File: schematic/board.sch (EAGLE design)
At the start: 4 parts, among them U1 STM32F103C8T6

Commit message: Кажется, все необходимое для МК нарисовано
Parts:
- added C1: 10uF, SparkFun-Capacitors:10UF-1206-6.3V-20%
- added C2: 100uF, SparkFun-Capacitors:10UF-1206-6.3V-20%
- added C3, C4: 8uF, SparkFun-Capacitors:22UF-0805-6.3V-20%
- added C5, C6: 7uF, SparkFun-Capacitors:22UF-0805-6.3V-20%
- added R1: 1.5kOhm, rcl:R-EU_R0603
- added R2: 0 Ohm, rcl:R-EU_R0603
- added X1: NX3215SA-32.768K, SparkFun-Clocks:CRYSTALSMD-3.2X1.5
- added X2: NX5032GA-8MHz, SparkFun-Clocks:CRYSTALSMD-5X3.2-2PAD
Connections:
- new net N$1: C4.2, U1.PD0_OSC_IN, X2.1
- new net N$2: R1.2, U1.PD1_OSC_OUT
- new net N$3: C6.1, R2.2, X1.1
- new net N$4: C3.2, R1.1, X2.2
- new net N$5: C5.1, U1.PC14-OSC32_IN, X1.2
- new net N$6: R2.1, U1.PC15-OSC32_OUT
- net +3V3: now also C1.1
- net +5V: now also C2.1
- net GND: now also C1.2, C2.2, C3.1, C4.1, C5.2, C6.2
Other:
- note added: "Все SMD конденсаторы в корпусахх 1206"

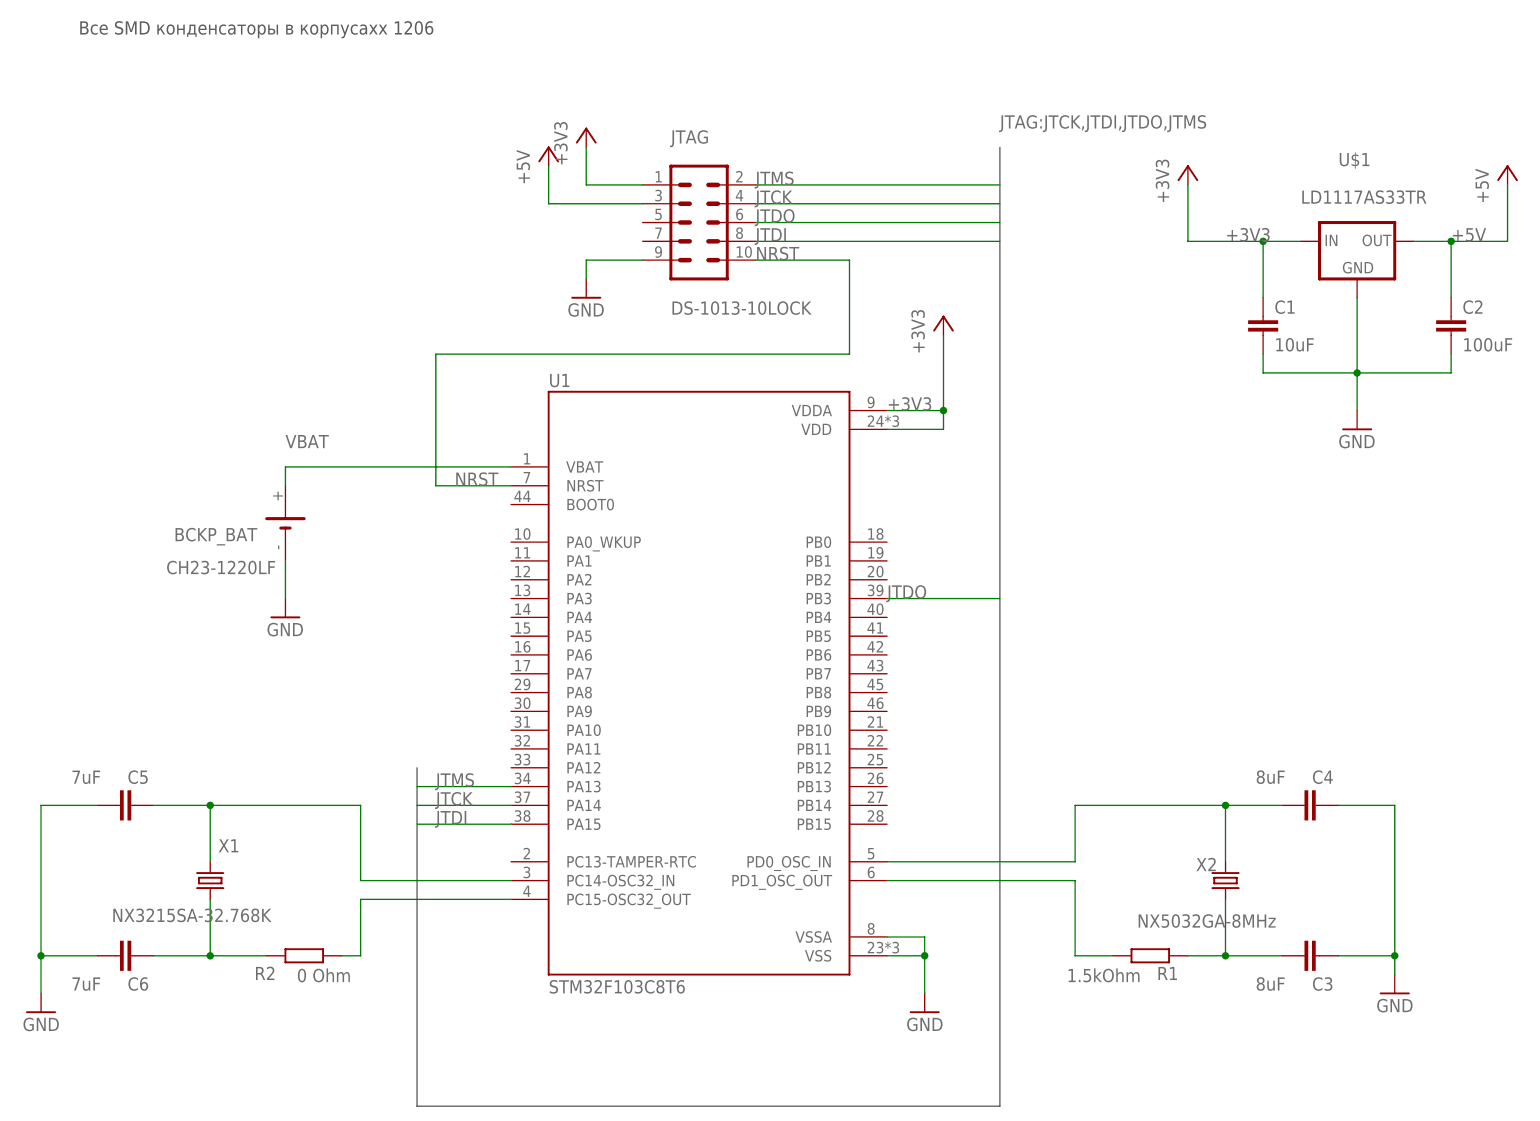
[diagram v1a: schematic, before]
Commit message: Начерно набросана обвязка мк (без фильтрующих кондеров). Обвязка МК нагло срисована с блюпила без номиналов
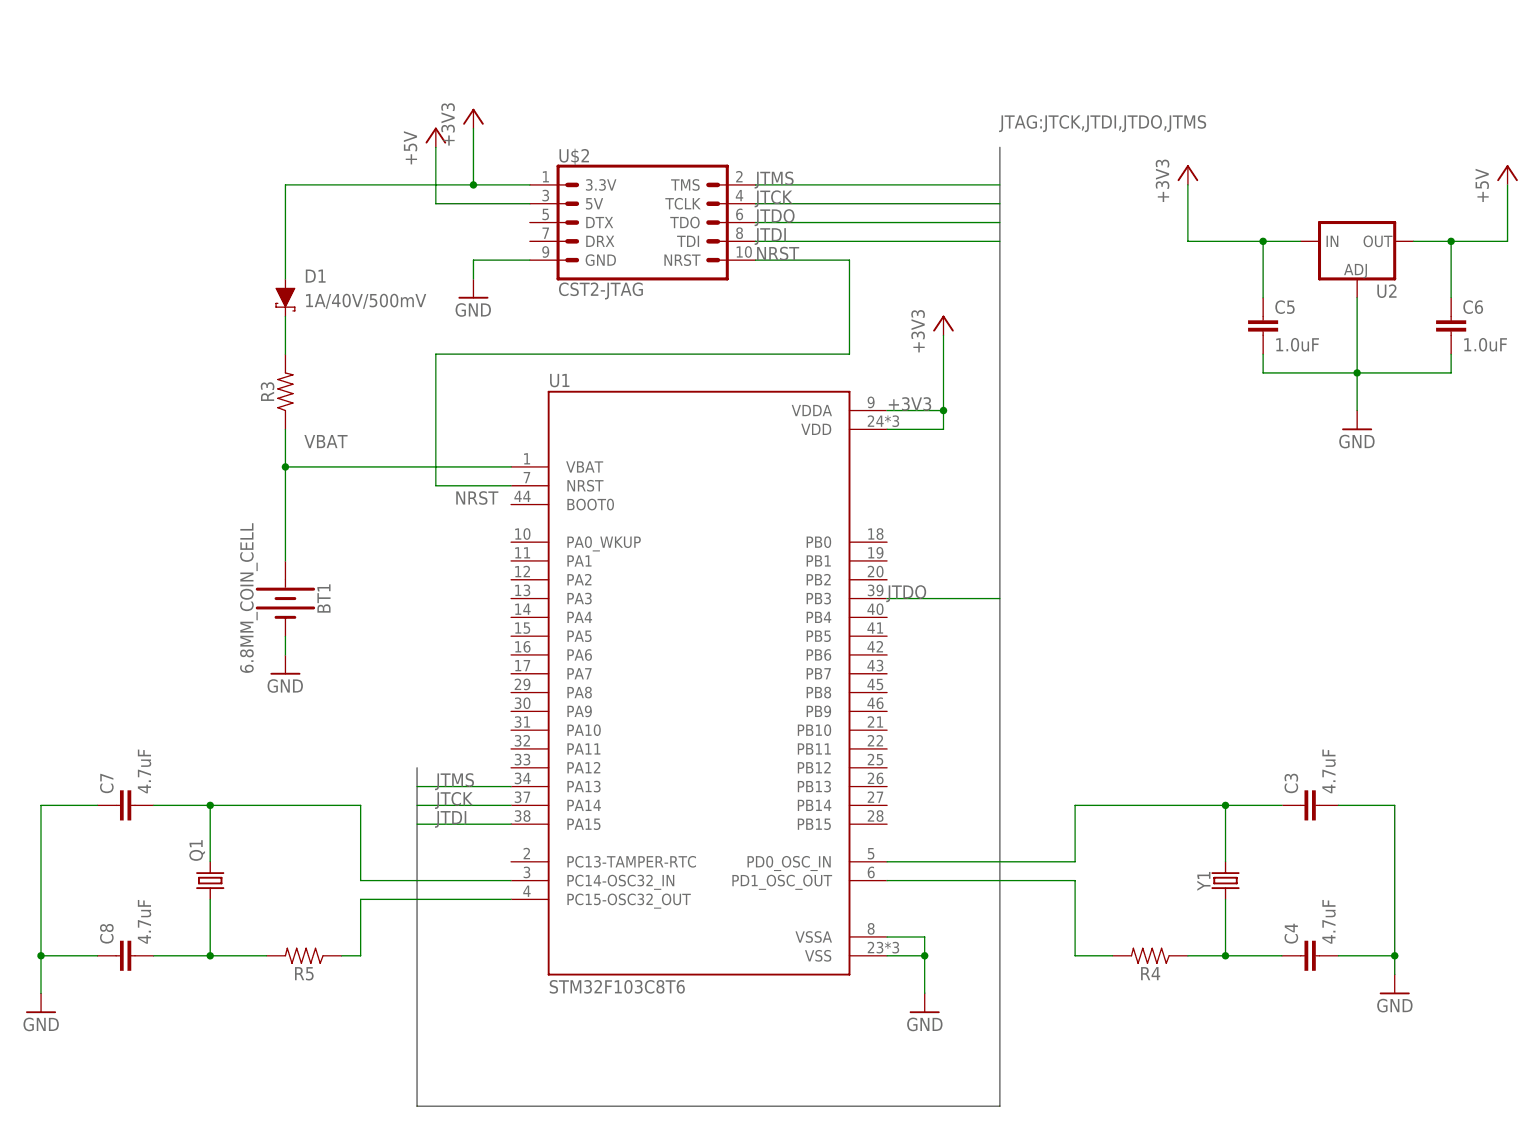
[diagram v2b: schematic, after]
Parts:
- removed BCKP_BAT: CH23-1220LF, battery:CH23-1220LF
- removed C1: 10uF, SparkFun-Capacitors:10UF-1206-6.3V-20%
- removed C2: 100uF, SparkFun-Capacitors:10UF-1206-6.3V-20%
- removed JTAG: DS-1013-10LOCK, IDC:DS-1013-10LOCK
- removed R1: 1.5kOhm, rcl:R-EU_R0603
- removed R2: 0 Ohm, rcl:R-EU_R0603
- removed U$1: LD1117AS33TR, VREG:LD1117AS33TRSOT-223
- removed X1: NX3215SA-32.768K, SparkFun-Clocks:CRYSTALSMD-3.2X1.5
- removed X2: NX5032GA-8MHz, SparkFun-Clocks:CRYSTALSMD-5X3.2-2PAD
- added BT1: 6.8MM_COIN_CELL, SparkFun-Batteries:BATTERY-6.8MM_SMD
- added C7, C8: 4.7uF, SparkFun-Capacitors:4.7UF-0603-35V-(20%)
- added D1: 1A/40V/500mV, SparkFun-DiscreteSemi:DIODE-SCHOTTKY-SS14
- added Q1: (no value), crystal:CRYSTALMM20SS
- added R3, R4, R5: (no value), SparkFun-Resistors:RESISTOR0603
- added U$2: CST2-JTAG, IDC:CST2-JTAG
- added U2: (no value), SparkFun-IC-Power:V_REG_LM1117SOT223
- added Y1: (no value), SparkFun-Clocks:CRYSTALPTH-HC49US
- C3, C4: value 8uF -> 4.7uF; device SparkFun-Capacitors:22UF-0805-6.3V-20% -> SparkFun-Capacitors:4.7UF-0603-35V-(20%)
- C5, C6: value 7uF -> 1.0uF; device SparkFun-Capacitors:22UF-0805-6.3V-20% -> SparkFun-Capacitors:1.0UF-0805-25V-10%
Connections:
- new net N$7: D1.C, R3.2
- net +3V3: now also C5.1, D1.A, U$2.3.3V, U2.IN; no longer C1.1, JTAG.1, U$1.IN
- net +5V: now also C6.1, U$2.5V, U2.OUT; no longer C2.1, JTAG.3, U$1.OUT
- net GND: now also BT1.-, C3.2, C4.2, C7.1, C8.1, U$2.GND, U2.ADJ; no longer BCKP_BAT.-, C1.2, C2.2, C3.1, C4.1, JTAG.9, U$1.GND
- net JTCK: now also U$2.TCLK; no longer JTAG.4
- net JTDI: now also U$2.TDI; no longer JTAG.8
- net JTDO: now also U$2.TDO; no longer JTAG.6
- net JTMS: now also U$2.TMS; no longer JTAG.2
- net N$1: now also C3.1, Y1.2; no longer C4.2, X2.1
- net N$2: now also R4.2; no longer R1.2
- net N$3: now also C8.2, Q1.1, R5.2; no longer C6.1, R2.2, X1.1
- net N$4: now also C4.1, R4.1, Y1.1; no longer C3.2, R1.1, X2.2
- net N$5: now also C7.2, Q1.2; no longer C5.1, X1.2
- net N$6: now also R5.1; no longer R2.1
- net NRST: now also U$2.NRST; no longer JTAG.10
- net VBAT: now also BT1.+, R3.1; no longer BCKP_BAT.+
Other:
- note removed: "Все SMD конденсаторы в корпусахх 1206"
- moved on the sheet: C3, C4, C5, C6

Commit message: Радиомодули LORA 433
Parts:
- removed R4, R5: (no value), SparkFun-Resistors:RESISTOR0603
- added R1, R2: (no value), SparkFun-Resistors:RESISTOR0603
- added U$1: E22-400M30S, ebyte-radio:E22-400M30S
- added U$3: E22-400M22S, ebyte-radio:E22-400M22S
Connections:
- removed net N$1: C3.1, U1.PD0_OSC_IN, Y1.2
- removed net N$2: R4.2, U1.PD1_OSC_OUT
- removed net N$3: C8.2, Q1.1, R5.2
- removed net N$4: C4.1, R4.1, Y1.1
- removed net N$5: C7.2, Q1.2, U1.PC14-OSC32_IN
- removed net N$6: R5.1, U1.PC15-OSC32_OUT
- new net E22-BUSY: U$1.BUSY, U$3.BUSY
- new net E22-CLK: U$1.SCK, U$3.SCK
- new net E22-CS: U$1.NSS, U$3.NSS
- new net E22-DIO1: U$1.DIO1, U$3.DIO1
- new net E22-DIO2: U$1.DIO2, U$3.DIO2
- new net E22-MISO: U$1.MISO, U$3.MISO
- new net E22-MOSI: U$1.MOSI, U$3.MOSI
- new net E22-NRST: U$1.NRST, U$3.NRST
- new net E22-RXEN: U$1.RXEN, U$3.RXEN
- new net E22-TXEN: U$1.TXEN, U$3.TXEN
- new net HSE-IN: C4.1, U1.PD0_OSC_IN, Y1.1
- new net HSE-OUT: R2.2, U1.PD1_OSC_OUT
- new net LSE-IN: C8.2, Q1.1, U1.PC14-OSC32_IN
- new net LSE-OUT: R1.1, U1.PC15-OSC32_OUT
- new net N$8: C7.2, Q1.2, R1.2
- new net N$9: C3.1, R2.1, Y1.2
- net +5V: now also U$1.VCC, U$3.VCC
- net GND: now also U$1.GND, U$3.GND
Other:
- moved on the sheet: BT1, C3, C4, C5, C6, C7, C8, D1, Q1, R3, U$2, U1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

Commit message: Модули для NRF24 в каком-то виде на платах
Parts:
- added U$4: E01-ML01SP4, ebyte-radio:E01-ML01SP4
- added U$5: E01-ML01DP5, ebyte-radio:E01-ML01DP5
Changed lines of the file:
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@@
 <part name="R1" library="SparkFun-Resistors" deviceset="RESISTOR" device="0603" value=" "/>
 <part name="R2" library="SparkFun-Resistors" deviceset="RESISTOR" device="0603" value=" "/>
+<part name="U$4" library="ebyte-radio" deviceset="E01-ML01SP4" device=""/>
+<part name="U$5" library="ebyte-radio" deviceset="E01-ML01DP5" device=""/>
 </parts>
 <sheets>
@@
 <attribute name="VALUE" x="-142.24" y="-72.136" size="1.778" layer="96" font="vector" rot="MR180" align="top-center"/>
 </instance>
+<instance part="U$4" gate="G$1" x="60.96" y="-30.48" smashed="yes">
+<attribute name="NAME" x="53.34" y="-17.78" size="1.27" layer="95"/>
+<attribute name="VALUE" x="53.34" y="-43.18" size="1.27" layer="96"/>
+</instance>
+<instance part="U$5" gate="G$1" x="132.08" y="-30.48" smashed="yes">
+<attribute name="NAME" x="124.46" y="-17.78" size="1.27" layer="95"/>
+<attribute name="VALUE" x="124.46" y="-43.18" size="1.27" layer="96"/>
+</instance>
 </instances>

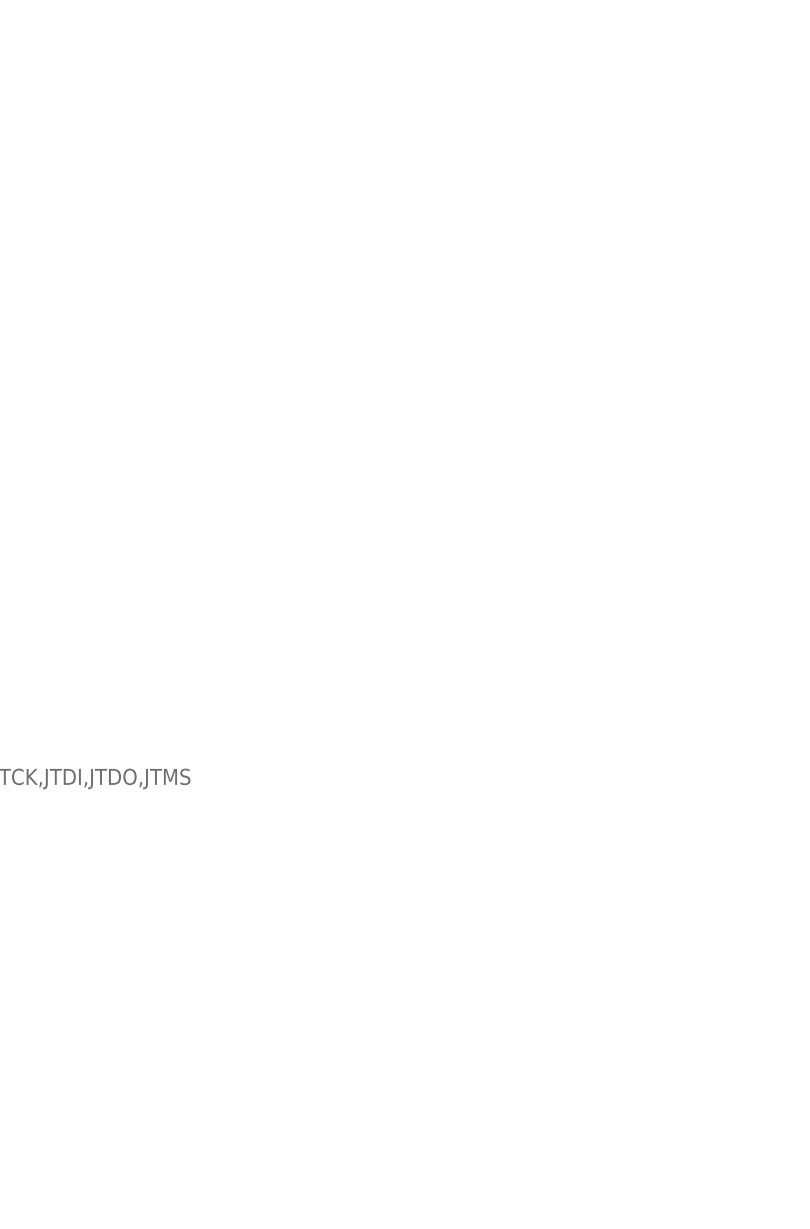
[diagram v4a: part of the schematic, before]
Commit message: Новый вариант разъема для отладки
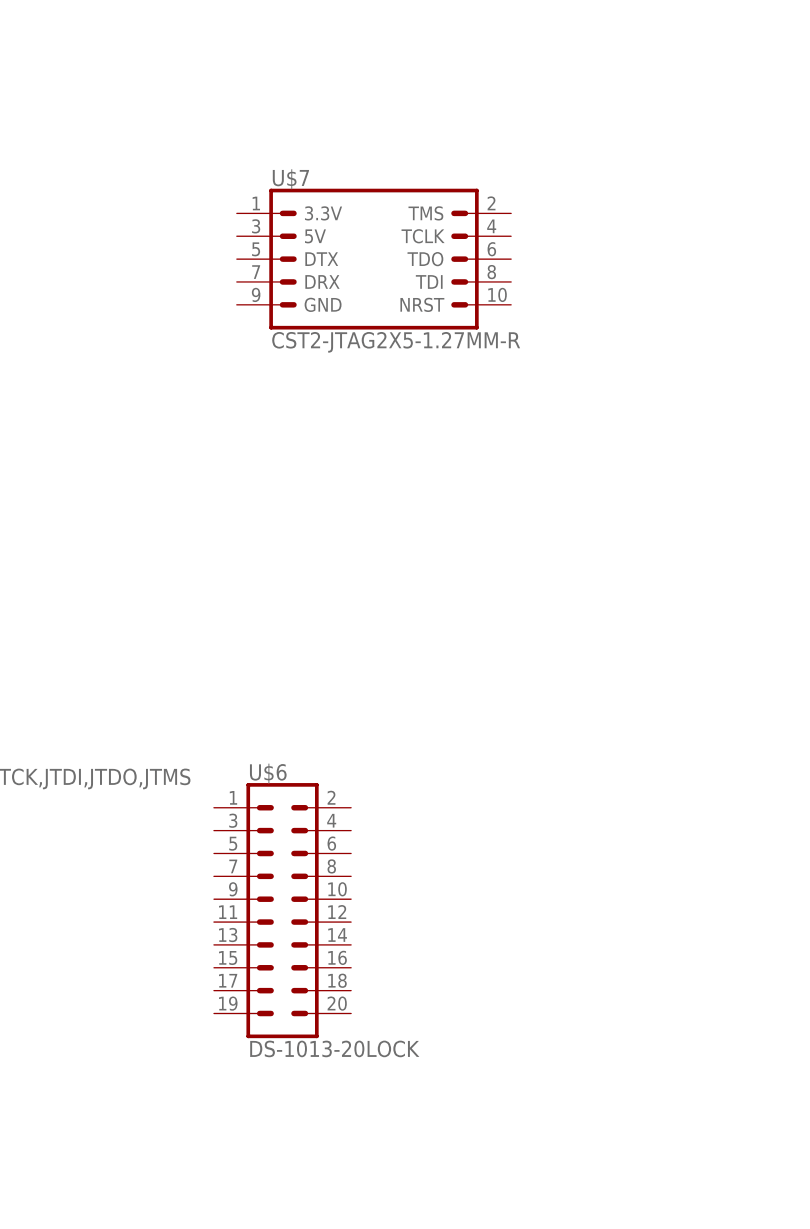
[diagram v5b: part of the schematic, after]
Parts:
- added U$6: DS-1013-20LOCK, IDC:DS-1013-20LOCK
- added U$7: CST2-JTAG2X5-1.27MM-R, IDC:CST2-JTAG2X5-1.27MM-R
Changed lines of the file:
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@@
 <part name="U$4" library="ebyte-radio" deviceset="E01-ML01SP4" device=""/>
 <part name="U$5" library="ebyte-radio" deviceset="E01-ML01DP5" device=""/>
+<part name="U$6" library="IDC" deviceset="DS-1013-20" device="LOCK"/>
+<part name="U$7" library="IDC" deviceset="CST2-JTAG" device="2X5-1.27MM-R"/>
 </parts>
 <sheets>
@@
 <attribute name="VALUE" x="124.46" y="-43.18" size="1.27" layer="96"/>
 </instance>
+<instance part="U$6" gate="G$1" x="-73.66" y="78.74" smashed="yes">
+<attribute name="VALUE" x="-77.47" y="61.214" size="1.778" layer="96" font="vector"/>
+<attribute name="NAME" x="-77.47" y="91.948" size="1.778" layer="95" font="vector"/>
+</instance>
+<instance part="U$7" gate="G$1" x="-63.5" y="149.86" smashed="yes">
+<attribute name="VALUE" x="-74.93" y="139.954" size="1.778" layer="96" font="vector"/>
+<attribute name="NAME" x="-74.93" y="157.988" size="1.778" layer="95" font="vector"/>
+</instance>
 </instances>
